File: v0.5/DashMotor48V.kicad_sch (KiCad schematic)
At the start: 108 parts, among them CN3(OUT)1 XT30(2+2)PB-M.G.B, CN3(OUT)2 XT30(2+2)PB-M.G.B, J1 BM07B-SRSS-TB(LF)(SN), J2 BM07B-SRSS-TB(LF)(SN), Q1 FDMT80080DC, Q2 FDMT80080DC, Q3 FDMT80080DC, Q4 FDMT80080DC, Q5 FDMT80080DC, Q6 FDMT80080DC, U1 STM32F446RET6, U2 DRV8353SRTAR, U3 MCP2542FD-E/MF, U4 MA732GQ-Z, U5 TPS629203DRLR, U6 TPS629203DRLR, Y1 CSTNE8M00G550000R0

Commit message: keep working on v05
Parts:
- added C44, C45: 100nF 50V, dash:CC0603JRX7R9BB104, symbol dash:CC0603JRX7R9BB104
- added J3: Conn_01x02_Pin, symbol Connector:Conn_01x02_Pin
- added R5: RT0402DRE0710KL, dash:RT0402DRE0710KL, symbol dash:RT0402DRE0710KL
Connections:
- net +3.3V: now also J3.2 (Pin_2)
- net GND: now also C44.1, C45.1, R5.1
- net VBAT: now reaches R1.2, R2.2, U1.15 (PA1)
- net VBAT: now also C45.2
- net I_C: now reaches U1.10 (PC2)
- net I_C: now also U2.21 (SOC)
- net VMOT_TEMP: now reaches U1.14 (PA0)
- net VMOT_TEMP: now also C44.2, J3.1 (Pin_1), R5.2
- no-connect marks 39 -> 36
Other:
- moved on the sheet: C1, C10, C11, C12, C13, C14, C15, C16, C17, C18, C19, C2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

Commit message: back up
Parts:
- removed C21: GRM32ER71J106KA12L, dash:GRM32ER71J106KA12L, symbol dash:GRM32ER71J106KA12L
- removed C22, C24, C28, C29, C30, C33, C34, C35, C36, C44, C45: 100nF 50V, dash:CC0603JRX7R9BB104, symbol dash:CC0603JRX7R9BB104
- added C21: GRM32EC72A106KE05L, dash:GRM32EC72A106KE05L, symbol dash:GRM32EC72A106KE05L
- added C24, C47, C48, C49, C50, C51, C52, C53, C54, C55, C56: 100nF 100V, dash:CL10B104KC8NNNC, symbol dash:CL10B104KC8NNNC
- added C46: CL31B105KCHNNNE, dash:CL31B105KCHNNNE, symbol dash:CL31B105KCHNNNE
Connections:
- net +12V: now also C21.2, C51.1
- net +3.3V: now also C46.2, C47.1, C48.1, C49.1, C50.1, C53.1, C54.1
- net +5V: now also C52.1
- net GND: now also C21.1, C24.2, C46.1, C47.2, C48.2, C49.2, C50.2, C51.2, C52.2, C53.2, C54.2, C55.2, C56.2
- net VBAT: now also C55.1
- net VMOT_TEMP: now also C56.1
- net at FL1.2, U1.13 (VDDA/VREF+): now also C24.1

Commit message: upload again
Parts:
- removed C25, C27, C32, C46: CL31B105KCHNNNE, dash:CL31B105KCHNNNE, symbol dash:CL31B105KCHNNNE
- added C22, C28, C29, C30: 1uF 100V, dash:GRM21BC72A105KE01L, symbol dash:GRM21BC72A105KE01L
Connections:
- net +3.3V: now also C22.2, C30.2
- net GND: now also C22.1, C28.1, C29.1, C30.1
- net at U2.38 (DVDD): now also C29.2
- net at U2.40 (VGLS): now also C28.2

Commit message: keep routing
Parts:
- removed R1: RC0402FR-07150KL, dash:RC0402FR_07150KL, symbol dash:RC0402FR_07150KL
- added R6: YAGEO RC0603FR-07200KL, dash:YAGEO RC0603FR-07200KL, symbol Device:R_US
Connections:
- net +48V: now also R6.1
- net VBAT: now also R6.2
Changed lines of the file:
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@@
 	(wire
 		(pts
+			(xy 396.24 156.21) (xy 396.24 166.37)
+		)
+		(stroke
+			(width 0)
+			(type default)
+		)
+	)
+	(wire
+		(pts
 			(xy 452.12 173.99) (xy 438.15 173.99)
 		)
@@
 	(wire
 		(pts
-			(xy 396.24 140.97) (xy 396.24 143.51)
-		)
-		(stroke
-			(width 0)
-			(type default)
-		)
-	)
-	(wire
-		(pts
 			(xy 135.89 321.31) (xy 135.89 325.12)
 		)
@@
 	(wire
 		(pts
+			(xy 396.24 140.97) (xy 396.24 148.59)
+		)
+		(stroke
+			(width 0)
+			(type default)
+		)
+	)
+	(wire
+		(pts
 			(xy 185.42 317.5) (xy 184.15 317.5)
 		)
@@
 	(wire
 		(pts
-			(xy 396.24 163.83) (xy 396.24 166.37)
-		)
-		(stroke
-			(width 0)
-			(type default)
-		)
-	)
-	(wire
-		(pts
 			(xy 391.16 85.09) (xy 391.16 88.9)
 		)
@@
 	)
 	(symbol
-		(lib_id "dash:RC0402FR_07150KL")
-		(at 396.24 153.67 270)
-		(unit 1)
-		(body_style 1)
-		(exclude_from_sim no)
-		(in_bom yes)
-		(on_board yes)
-		(in_pos_files yes)
-		(dnp no)
-		(property "Reference" "R1"
-			(at 402.59 153.67 0)
-			(show_name no)
-			(do_not_autoplace no)
-			(effects
-				(font
-					(size 1.27 1.27)
-				)
-			)
-		)
-		(property "Value" "RC0402FR-07150KL"
-			(at 400.05 153.67 0)
-			(hide yes)
-			(show_name no)
-			(do_not_autoplace no)
-			(effects
-				(font
-					(size 1.27 1.27)
-				)
-			)
-		)
-		(property "Footprint" "dash:RC0402FR_07150KL"
-			(at 396.24 153.67 0)
-			(hide yes)
-			(show_name no)
-			(do_not_autoplace no)
-			(effects
-				(font
-					(size 1.27 1.27)
-				)
-				(justify bottom)
-			)
-		)
-		(property "Datasheet" "https://www.lcsc.com/product-detail/C93947.html"
-			(at 396.24 153.67 0)
-			(hide yes)
-			(show_name no)
-			(do_not_autoplace no)
-			(effects
-				(font
-					(size 1.27 1.27)
-				)
-			)
-		)
-		(property "Description" "150K 1%"
-			(at 399.796 153.67 0)
-			(show_name no)
-			(do_not_autoplace no)
-			(effects
-				(font
-					(size 1.27 1.27)
-				)
-			)
-		)
-		(pin "1"
-		)
-		(pin "2"
-		)
-		(instances
-			(project "DashMotor48V"
-				(path "/71f0fcc1-c7ad-470c-8d48-d038c53969d3"
-					(reference "R1")
-					(unit 1)
-				)
-			)
-		)
-	)
-	(symbol
 		(lib_id "power:+3.3V")
 		(at 237.49 251.46 0)
@@
 	)
 	(symbol
+		(lib_id "Device:R_US")
+		(at 396.24 152.4 0)
+		(unit 1)
+		(body_style 1)
+		(exclude_from_sim no)
+		(in_bom yes)
+		(on_board yes)
+		(in_pos_files yes)
+		(dnp no)
+		(property "Reference" "R6"
+			(at 398.78 151.1299 0)
+			(show_name no)
+			(do_not_autoplace no)
+			(effects
+				(font
+					(size 1.27 1.27)
+				)
+				(justify left)
+			)
+		)
+		(property "Value" "YAGEO RC0603FR-07200KL"
+			(at 398.78 153.6699 0)
+			(hide yes)
+			(show_name no)
+			(do_not_autoplace no)
+			(effects
+				(font
+					(size 1.27 1.27)
+				)
+				(justify left)
+			)
+		)
+		(property "Footprint" "dash:YAGEO RC0603FR-07200KL"
+			(at 397.256 152.654 90)
+			(hide yes)
+			(show_name no)
+			(do_not_autoplace no)
+			(effects
+				(font
+					(size 1.27 1.27)
+				)
+			)
+		)
+		(property "Datasheet" "YAGEO RC0603FR-07200KL"
+			(at 396.24 152.4 0)
+			(hide yes)
+			(show_name no)
+			(do_not_autoplace no)
+			(effects
+				(font
+					(size 1.27 1.27)
+				)
+			)
+		)
+		(property "Description" "200K 1%"
+			(at 402.59 154.432 0)
+			(show_name no)
+			(do_not_autoplace no)
+			(effects
+				(font
+					(size 1.27 1.27)
+				)
+			)
+		)
+		(pin "2"
+		)
+		(pin "1"
+		)
+		(instances
+			(project "DashMotor48V"
+				(path "/71f0fcc1-c7ad-470c-8d48-d038c53969d3"
+					(reference "R6")
+					(unit 1)
+				)
+			)
+		)
+	)
+	(symbol
 		(lib_id "power:+3.3V")
 		(at 156.21 53.34 0)
@@
 		(in_pos_files yes)
 		(dnp no)
-		(fields_autoplaced yes)
 		(property "Reference" "#PWR046"
 			(at 464.82 257.81 0)
@@
 		)
 		(property "Value" "GND"
-			(at 464.82 256.54 0)
+			(at 462.534 255.524 0)
 			(show_name no)
 			(do_not_autoplace no)
@@
 		(in_pos_files yes)
 		(dnp no)
-		(fields_autoplaced yes)
 		(property "Reference" "#PWR053"
 			(at 469.9 265.43 0)
@@
 		)
 		(property "Value" "+48V"
-			(at 469.9 256.54 0)
+			(at 470.154 257.302 0)
 			(show_name no)
 			(do_not_autoplace no)

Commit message: keep routing
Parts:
- removed C31: 100nF 50V, dash:CC0603JRX7R9BB104, symbol dash:CC0603JRX7R9BB104
- added C57: 100nF 100V, dash:CL10B104KC8NNNC, symbol dash:CL10B104KC8NNNC
- J3: footprint (none) -> Connector_PinHeader_2.54mm:PinHeader_1x02_P2.54mm_Vertical
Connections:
- net +3.3V: now also C57.1
- net CAN+: now also CN3(OUT)1.2, CN3(OUT)2.2; no longer CN3(OUT)1.1, CN3(OUT)2.1
- net CAN-: now also CN3(OUT)1.1, CN3(OUT)2.1; no longer CN3(OUT)1.2, CN3(OUT)2.2
- net GND: now also C57.2
- net I_A: now also U1.10 (PC2); no longer U1.8 (PC0)
- net I_C: now also U1.8 (PC0); no longer U1.10 (PC2)
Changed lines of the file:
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@@
 		)
 	)
-	(label "CAN-"
+	(label "CAN+"
 		(at 464.82 248.92 0)
 		(effects
@@
 		)
 	)
-	(label "CAN+"
+	(label "CAN-"
 		(at 464.82 246.38 0)
 		(effects
@@
 		)
 	)
-	(label "I_A"
+	(label "I_C"
 		(at 90.17 71.12 0)
 		(effects
@@
 		)
 	)
-	(label "I_C"
+	(label "I_A"
 		(at 90.17 76.2 0)
 		(effects
@@
 		)
 	)
-	(label "CAN-"
+	(label "CAN+"
 		(at 491.49 248.92 0)
 		(effects
@@
 		)
 	)
-	(label "CAN+"
+	(label "CAN-"
 		(at 491.49 246.38 0)
 		(effects
@@
 			)
 		)
-		(property "Footprint" ""
+		(property "Footprint" "Connector_PinHeader_2.54mm:PinHeader_1x02_P2.54mm_Vertical"
 			(at 447.04 148.59 0)
 			(hide yes)
@@
 	)
 	(symbol
-		(lib_id "dash:CC0603JRX7R9BB104")
-		(at 170.18 154.94 270)
-		(unit 1)
-		(body_style 1)
-		(exclude_from_sim no)
-		(in_bom yes)
-		(on_board yes)
-		(in_pos_files yes)
-		(dnp no)
-		(fields_autoplaced yes)
-		(property "Reference" "C31"
-			(at 173.99 154.9399 90)
-			(show_name no)
-			(do_not_autoplace no)
-			(effects
-				(font
-					(size 1.27 1.27)
-				)
-				(justify left)
-			)
-		)
-		(property "Value" "100nF 50V"
-			(at 173.99 157.4799 90)
-			(show_name no)
-			(do_not_autoplace no)
-			(effects
-				(font
-					(size 1.27 1.27)
-				)
-				(justify left)
-			)
-		)
-		(property "Footprint" "dash:CC0603JRX7R9BB104"
-			(at 170.18 154.94 0)
-			(hide yes)
-			(show_name no)
-			(do_not_autoplace no)
-			(effects
-				(font
-					(size 1.27 1.27)
-				)
-				(justify bottom)
-			)
-		)
-		(property "Datasheet" ""
-			(at 170.18 154.94 0)
-			(hide yes)
-			(show_name no)
-			(do_not_autoplace no)
-			(effects
-				(font
-					(size 1.27 1.27)
-				)
-			)
-		)
-		(property "Description" ""
-			(at 170.18 154.94 0)
-			(hide yes)
-			(show_name no)
-			(do_not_autoplace no)
-			(effects
-				(font
-					(size 1.27 1.27)
-				)
-			)
-		)
-		(pin "2"
-		)
-		(pin "1"
-		)
-		(instances
-			(project "DashMotor48V"
-				(path "/71f0fcc1-c7ad-470c-8d48-d038c53969d3"
-					(reference "C31")
-					(unit 1)
-				)
-			)
-		)
-	)
-	(symbol
 		(lib_id "dash:GRM32EC72A106KE05L")
 		(at 491.49 41.91 90)
@@
 					(unit 1)
 				)
+			)
+		)
+	)
+	(symbol
+		(lib_id "dash:CL10B104KC8NNNC")
+		(at 170.18 154.94 270)
+		(unit 1)
+		(body_style 1)
+		(exclude_from_sim no)
+		(in_bom yes)
+		(on_board yes)
+		(in_pos_files yes)
+		(dnp no)
+		(property "Reference" "C57"
+			(at 174.752 151.638 0)
+			(show_name no)
+			(do_not_autoplace no)
+			(effects
+				(font
+					(size 1.27 1.27)
+				)
+			)
+		)
+		(property "Value" "100nF 100V"
+			(at 172.72 155.702 0)
+			(show_name no)
+			(do_not_autoplace no)
+			(effects
+				(font
+					(size 1.27 1.27)
+				)
+			)
+		)
+		(property "Footprint" "dash:CL10B104KC8NNNC"
+			(at 170.18 154.94 0)
+			(hide yes)
+			(show_name no)
+			(do_not_autoplace no)
+			(effects
+				(font
+					(size 1.27 1.27)
+				)
+				(justify bottom)
+			)
+		)
+		(property "Datasheet" ""
+			(at 170.18 154.94 0)
+			(hide yes)
+			(show_name no)
+			(do_not_autoplace no)
+			(effects
+				(font
+					(size 1.27 1.27)
+				)
+			)
+		)
+		(property "Description" ""
+			(at 170.18 154.94 0)
+			(hide yes)
+			(show_name no)
+			(do_not_autoplace no)
+			(effects
+				(font
+					(size 1.27 1.27)
+				)
+			)
+		)
+		(property "E_max" "0.9"
+			(at 170.18 154.94 0)
+			(hide yes)
+			(show_name no)
+			(do_not_autoplace no)
+			(effects
+				(font
+					(size 1.27 1.27)
+				)
+				(justify bottom)
+			)
+		)
+		(property "L_max" "0.5"
+			(at 170.18 154.94 0)
+			(hide yes)
+			(show_name no)
+			(do_not_autoplace no)
+			(effects
+				(font
+					(size 1.27 1.27)
+				)
+				(justify bottom)
+			)
+		)
+		(property "A_max" "0.9"
+			(at 170.18 154.94 0)
+			(hide yes)
+			(show_name no)
+			(do_not_autoplace no)
+			(effects
+				(font
+					(size 1.27 1.27)
+				)
+				(justify bottom)
+			)
+		)
+		(property "L1_nom" "0.3"
+			(at 170.18 154.94 0)
+			(hide yes)
+			(show_name no)
+			(do_not_autoplace no)
+			(effects
+				(font
+					(size 1.27 1.27)
+				)
+				(justify bottom)
+			)
+		)
+		(property "D_max" "1.7"
+			(at 170.18 154.94 0)
+			(hide yes)
+			(show_name no)
+			(do_not_autoplace no)
+			(effects
+				(font
+					(size 1.27 1.27)
+				)
+				(justify bottom)
+			)
+		)
+		(property "A_nom" "0.9"
+			(at 170.18 154.94 0)
+			(hide yes)
+			(show_name no)
+			(do_not_autoplace no)
+			(effects
+				(font
+					(size 1.27 1.27)
+				)
+				(justify bottom)
+			)
+		)
+		(property "L1_max" "0.5"
+			(at 170.18 154.94 0)
+			(hide yes)
+			(show_name no)
+			(do_not_autoplace no)
+			(effects
+				(font
+					(size 1.27 1.27)
+				)
+				(justify bottom)
+			)
+		)
+		(property "L1_min" "0.1"
+			(at 170.18 154.94 0)
+			(hide yes)
+			(show_name no)
+			(do_not_autoplace no)
+			(effects
+				(font
+					(size 1.27 1.27)
+				)
+				(justify bottom)
+			)
+		)
+		(property "A_min" "0.9"
+			(at 170.18 154.94 0)
+			(hide yes)
+			(show_name no)
+			(do_not_autoplace no)
+			(effects
+				(font
+					(size 1.27 1.27)
+				)
+				(justify bottom)
+			)
+		)
+		(property "E_min" "0.7"
+			(at 170.18 154.94 0)
+			(hide yes)
+			(show_name no)
+			(do_not_autoplace no)
+			(effects
+				(font
+					(size 1.27 1.27)
+				)
+				(justify bottom)
+			)
+		)
+		(property "D_min" "1.5"
+			(at 170.18 154.94 0)
+			(hide yes)
+			(show_name no)
+			(do_not_autoplace no)
+			(effects
+				(font
+					(size 1.27 1.27)
+				)
+				(justify bottom)
+			)
+		)
+		(property "D_nom" "1.6"
+			(at 170.18 154.94 0)
+			(hide yes)
+			(show_name no)
+			(do_not_autoplace no)
+			(effects
+				(font
+					(size 1.27 1.27)
+				)
+				(justify bottom)
+			)
+		)
+		(property "E_nom" "0.8"
+			(at 170.18 154.94 0)
+			(hide yes)
+			(show_name no)
+			(do_not_autoplace no)
+			(effects
+				(font
+					(size 1.27 1.27)
+				)
+				(justify bottom)
+			)
+		)
+		(property "STANDARD" "IPC 7351B"
+			(at 170.18 154.94 0)
+			(hide yes)
+			(show_name no)
+			(do_not_autoplace no)
+			(effects
+				(font
+					(size 1.27 1.27)
+				)
+				(justify bottom)
+			)
+		)
+		(property "L_min" "0.1"
+			(at 170.18 154.94 0)
+			(hide yes)
+			(show_name no)
+			(do_not_autoplace no)
+			(effects
+				(font
+					(size 1.27 1.27)
+				)
+				(justify bottom)
+			)
+		)
+		(property "L_nom" "0.3"
+			(at 170.18 154.94 0)
+			(hide yes)
+			(show_name no)
+			(do_not_autoplace no)
+			(effects
+				(font
+					(size 1.27 1.27)
+				)
+				(justify bottom)
+			)
+		)
+		(property "MANUFACTURER" "Samsung Electro-Mechanics"
+			(at 170.18 154.94 0)
+			(hide yes)
+			(show_name no)
+			(do_not_autoplace no)
+			(effects
+				(font
+					(size 1.27 1.27)
+				)
+				(justify bottom)
+			)
+		)
+		(pin "2"
+		)
+		(pin "1"
+		)
+		(instances
+			(project "DashMotor48V"
+				(path "/71f0fcc1-c7ad-470c-8d48-d038c53969d3"
+					(reference "C57")
+					(unit 1)
+				)

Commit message: finish first draft
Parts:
- removed TP2: +48V TestPoint, TestPoint:TestPoint_THTPad_D1.5mm_Drill0.7mm, symbol Connector:TestPoint
- removed TP_GND1: GND TestPoint, TestPoint:TestPoint_THTPad_D1.5mm_Drill0.7mm, symbol Connector:TestPoint
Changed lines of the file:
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@@
 	)
 	(junction
-		(at 35.56 304.8)
-		(diameter 0)
-		(color 0 0 0 0)
-	)
-	(junction
 		(at 135.89 345.44)
 		(diameter 0)
@@
 	)
 	(junction
-		(at 184.15 344.17)
-		(diameter 0)
-		(color 0 0 0 0)
-	)
-	(junction
 		(at 435.61 59.69)
 		(diameter 0)
@@
 	(wire
 		(pts
-			(xy 184.15 344.17) (xy 184.15 346.71)
+			(xy 184.15 340.36) (xy 184.15 346.71)
 		)
 		(stroke
@@
 	(wire
 		(pts
-			(xy 184.15 340.36) (xy 184.15 344.17)
-		)
-		(stroke
-			(width 0)
-			(type default)
-		)
-	)
-	(wire
-		(pts
 			(xy 62.23 342.9) (xy 46.99 342.9)
 		)
@@
 	(wire
 		(pts
-			(xy 30.48 304.8) (xy 35.56 304.8)
+			(xy 30.48 304.8) (xy 38.1 304.8)
 		)
 		(stroke
@@
 	(wire
 		(pts
-			(xy 35.56 304.8) (xy 38.1 304.8)
-		)
-		(stroke
-			(width 0)
-			(type default)
-		)
-	)
-	(wire
-		(pts
 			(xy 90.17 104.14) (xy 102.87 104.14)
 		)
@@
 	)
 	(symbol
-		(lib_id "Connector:TestPoint")
-		(at 35.56 304.8 0)
-		(unit 1)
-		(body_style 1)
-		(exclude_from_sim no)
-		(in_bom yes)
-		(on_board yes)
-		(in_pos_files yes)
-		(dnp no)
-		(fields_autoplaced yes)
-		(property "Reference" "TP2"
-			(at 38.1 300.2279 0)
-			(show_name no)
-			(do_not_autoplace no)
-			(effects
-				(font
-					(size 1.27 1.27)
-				)
-				(justify left)
-			)
-		)
-		(property "Value" "+48V TestPoint"
-			(at 38.1 302.7679 0)
-			(show_name no)
-			(do_not_autoplace no)
-			(effects
-				(font
-					(size 1.27 1.27)
-				)
-				(justify left)
-			)
-		)
-		(property "Footprint" "TestPoint:TestPoint_THTPad_D1.5mm_Drill0.7mm"
-			(at 40.64 304.8 0)
-			(hide yes)
-			(show_name no)
-			(do_not_autoplace no)
-			(effects
-				(font
-					(size 1.27 1.27)
-				)
-			)
-		)
-		(property "Datasheet" ""
-			(at 40.64 304.8 0)
-			(hide yes)
-			(show_name no)
-			(do_not_autoplace no)
-			(effects
-				(font
-					(size 1.27 1.27)
-				)
-			)
-		)
-		(property "Description" "test point"
-			(at 35.56 304.8 0)
-			(hide yes)
-			(show_name no)
-			(do_not_autoplace no)
-			(effects
-				(font
-					(size 1.27 1.27)
-				)
-			)
-		)
-		(pin "1"
-		)
-		(instances
-			(project "DashMotor48V"
-				(path "/71f0fcc1-c7ad-470c-8d48-d038c53969d3"
-					(reference "TP2")
-					(unit 1)
-				)
-			)
-		)
-	)
-	(symbol
 		(lib_id "power:+5V")
 		(at 203.2 246.38 0)
@@
 					(unit 1)
 				)
-			)
-		)
-	)
-	(symbol
-		(lib_id "Connector:TestPoint")
-		(at 184.15 344.17 270)
-		(unit 1)
-		(body_style 1)
-		(exclude_from_sim no)
-		(in_bom yes)
-		(on_board yes)
-		(in_pos_files yes)
-		(dnp no)
-		(fields_autoplaced yes)
-		(property "Reference" "TP_GND1"
-			(at 189.23 342.8999 90)
-			(show_name no)
-			(do_not_autoplace no)
-			(effects
-				(font
-					(size 1.27 1.27)
-				)
-				(justify left)
-			)
-		)
-		(property "Value" "GND TestPoint"
-			(at 189.23 345.4399 90)
-			(show_name no)
-			(do_not_autoplace no)
-			(effects
-				(font
-					(size 1.27 1.27)
-				)
-				(justify left)
-			)
-		)
-		(property "Footprint" "TestPoint:TestPoint_THTPad_D1.5mm_Drill0.7mm"
-			(at 184.15 349.25 0)
-			(hide yes)
-			(show_name no)
-			(do_not_autoplace no)
-			(effects
-				(font
-					(size 1.27 1.27)
-				)
-			)
-		)
-		(property "Datasheet" ""
-			(at 184.15 349.25 0)
-			(hide yes)
-			(show_name no)
-			(do_not_autoplace no)
-			(effects
-				(font
-					(size 1.27 1.27)
-				)
-			)
-		)
-		(property "Description" "test point"
-			(at 184.15 344.17 0)
-			(hide yes)
-			(show_name no)
-			(do_not_autoplace no)
-			(effects
-				(font
-					(size 1.27 1.27)
-				)
-			)
-		)
-		(pin "1"
-		)
-		(instances
-			(project "DashMotor48V"
-				(path "/71f0fcc1-c7ad-470c-8d48-d038c53969d3"
-					(reference "TP_GND1")
-					(unit 1)
-				)

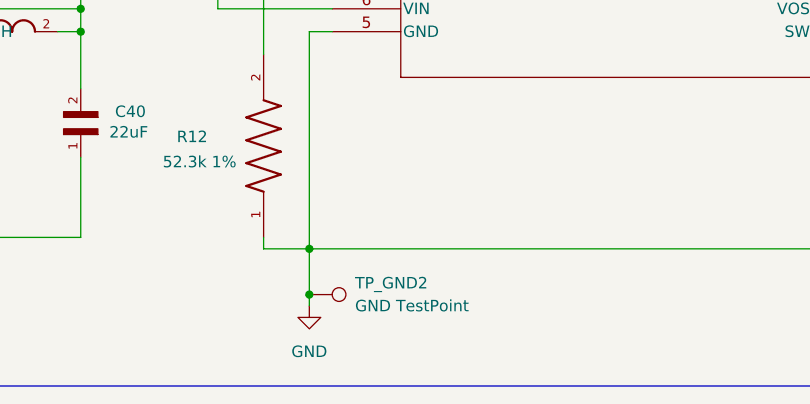
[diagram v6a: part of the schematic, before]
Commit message: adding more copper to the board
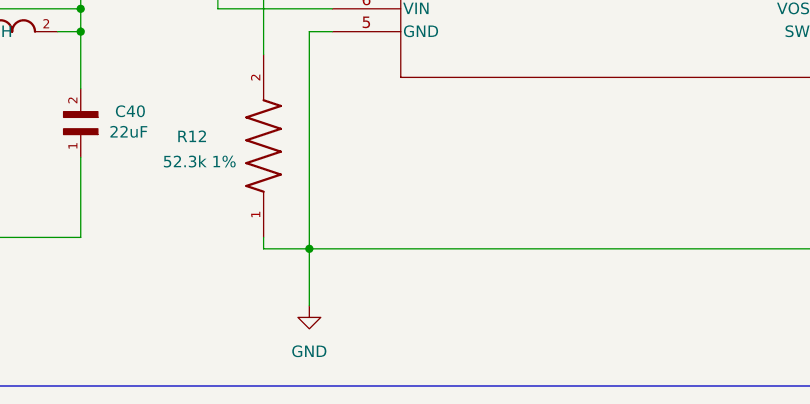
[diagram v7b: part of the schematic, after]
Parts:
- removed TP_GND2: GND TestPoint, TestPoint:TestPoint_THTPad_D1.5mm_Drill0.7mm, symbol Connector:TestPoint
- TP12, TP5, TP6: footprint TestPoint:TestPoint_THTPad_D1.0mm_Drill0.5mm -> TestPoint:TestPoint_Pad_D1.0mm
- TP3: footprint TestPoint:TestPoint_THTPad_D1.5mm_Drill0.7mm -> TestPoint:TestPoint_Pad_D1.0mm
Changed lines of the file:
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@@
 	)
 	(junction
-		(at 295.91 346.71)
-		(diameter 0)
-		(color 0 0 0 0)
-	)
-	(junction
 		(at 270.51 317.5)
 		(diameter 0)
@@
 	(wire
 		(pts
-			(xy 295.91 341.63) (xy 295.91 346.71)
-		)
-		(stroke
-			(width 0)
-			(type default)
-		)
-	)
-	(wire
-		(pts
 			(xy 392.43 36.83) (xy 400.05 36.83)
 		)
@@
 	(wire
 		(pts
-			(xy 295.91 346.71) (xy 295.91 347.98)
+			(xy 295.91 341.63) (xy 295.91 347.98)
 		)
 		(stroke
@@
 			)
 		)
-		(property "Footprint" "TestPoint:TestPoint_THTPad_D1.0mm_Drill0.5mm"
+		(property "Footprint" "TestPoint:TestPoint_Pad_D1.0mm"
 			(at 158.75 60.96 0)
 			(hide yes)
@@
 			)
 		)
-		(property "Footprint" "TestPoint:TestPoint_THTPad_D1.0mm_Drill0.5mm"
+		(property "Footprint" "TestPoint:TestPoint_Pad_D1.0mm"
 			(at 85.09 261.62 0)
 			(hide yes)
@@
 			)
 		)
-		(property "Footprint" "TestPoint:TestPoint_THTPad_D1.0mm_Drill0.5mm"
+		(property "Footprint" "TestPoint:TestPoint_Pad_D1.0mm"
 			(at 167.64 58.42 0)
 			(hide yes)
@@
 			)
 		)
-		(property "Footprint" "TestPoint:TestPoint_THTPad_D1.5mm_Drill0.7mm"
+		(property "Footprint" "TestPoint:TestPoint_Pad_D1.0mm"
 			(at 270.51 313.69 0)
 			(hide yes)
@@
 					(unit 1)
 				)
-			)
-		)
-	)
-	(symbol
-		(lib_id "Connector:TestPoint")
-		(at 295.91 346.71 270)
-		(unit 1)
-		(body_style 1)
-		(exclude_from_sim no)
-		(in_bom yes)
-		(on_board yes)
-		(in_pos_files yes)
-		(dnp no)
-		(fields_autoplaced yes)
-		(property "Reference" "TP_GND2"
-			(at 300.99 345.4399 90)
-			(show_name no)
-			(do_not_autoplace no)
-			(effects
-				(font
-					(size 1.27 1.27)
-				)
-				(justify left)
-			)
-		)
-		(property "Value" "GND TestPoint"
-			(at 300.99 347.9799 90)
-			(show_name no)
-			(do_not_autoplace no)
-			(effects
-				(font
-					(size 1.27 1.27)
-				)
-				(justify left)
-			)
-		)
-		(property "Footprint" "TestPoint:TestPoint_THTPad_D1.5mm_Drill0.7mm"
-			(at 295.91 351.79 0)
-			(hide yes)
-			(show_name no)
-			(do_not_autoplace no)
-			(effects
-				(font
-					(size 1.27 1.27)
-				)
-			)
-		)
-		(property "Datasheet" ""
-			(at 295.91 351.79 0)
-			(hide yes)
-			(show_name no)
-			(do_not_autoplace no)
-			(effects
-				(font
-					(size 1.27 1.27)
-				)
-			)
-		)
-		(property "Description" "test point"
-			(at 295.91 346.71 0)
-			(hide yes)
-			(show_name no)
-			(do_not_autoplace no)
-			(effects
-				(font
-					(size 1.27 1.27)
-				)
-			)
-		)
-		(pin "1"
-		)
-		(instances
-			(project "DashMotor48V"
-				(path "/71f0fcc1-c7ad-470c-8d48-d038c53969d3"
-					(reference "TP_GND2")
-					(unit 1)
-				)
